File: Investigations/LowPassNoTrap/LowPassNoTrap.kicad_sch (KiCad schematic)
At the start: 8 parts

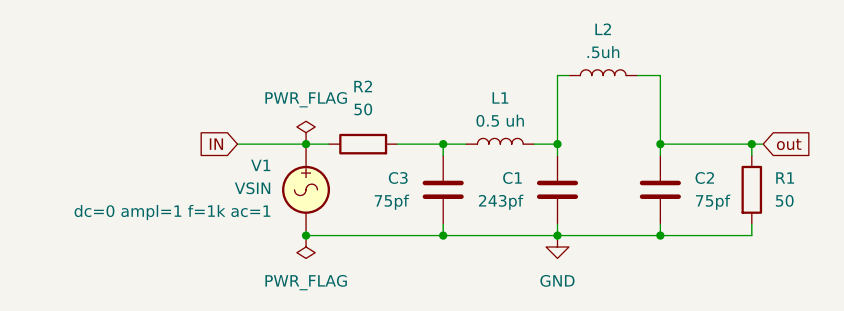
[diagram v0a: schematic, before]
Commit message: Simulations of Low Pass Filter + Harmonic Trap
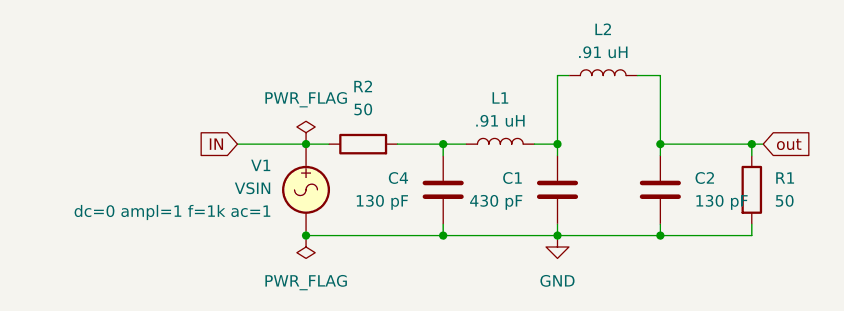
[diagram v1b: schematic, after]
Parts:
- C1: value 243pf -> 430 pF
- C2: value 75pf -> 130 pF
- C4: renamed from C3; value 75pf -> 130 pF
- L1: value 0.5 uh -> .91 uH
- L2: value .5uh -> .91 uH
